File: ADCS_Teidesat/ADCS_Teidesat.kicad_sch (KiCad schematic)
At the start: 27 parts, among them IC2 L86-M33, IC3 MAX2659ELT+T, IC4 THVD1400DR, IC5 TMS5703137DPGEQQ1, IC7 LSM6DSV16XTR, IC8 LIS2MDLTR, Y1 ATX-H13-F-16.000MHz-G100-T

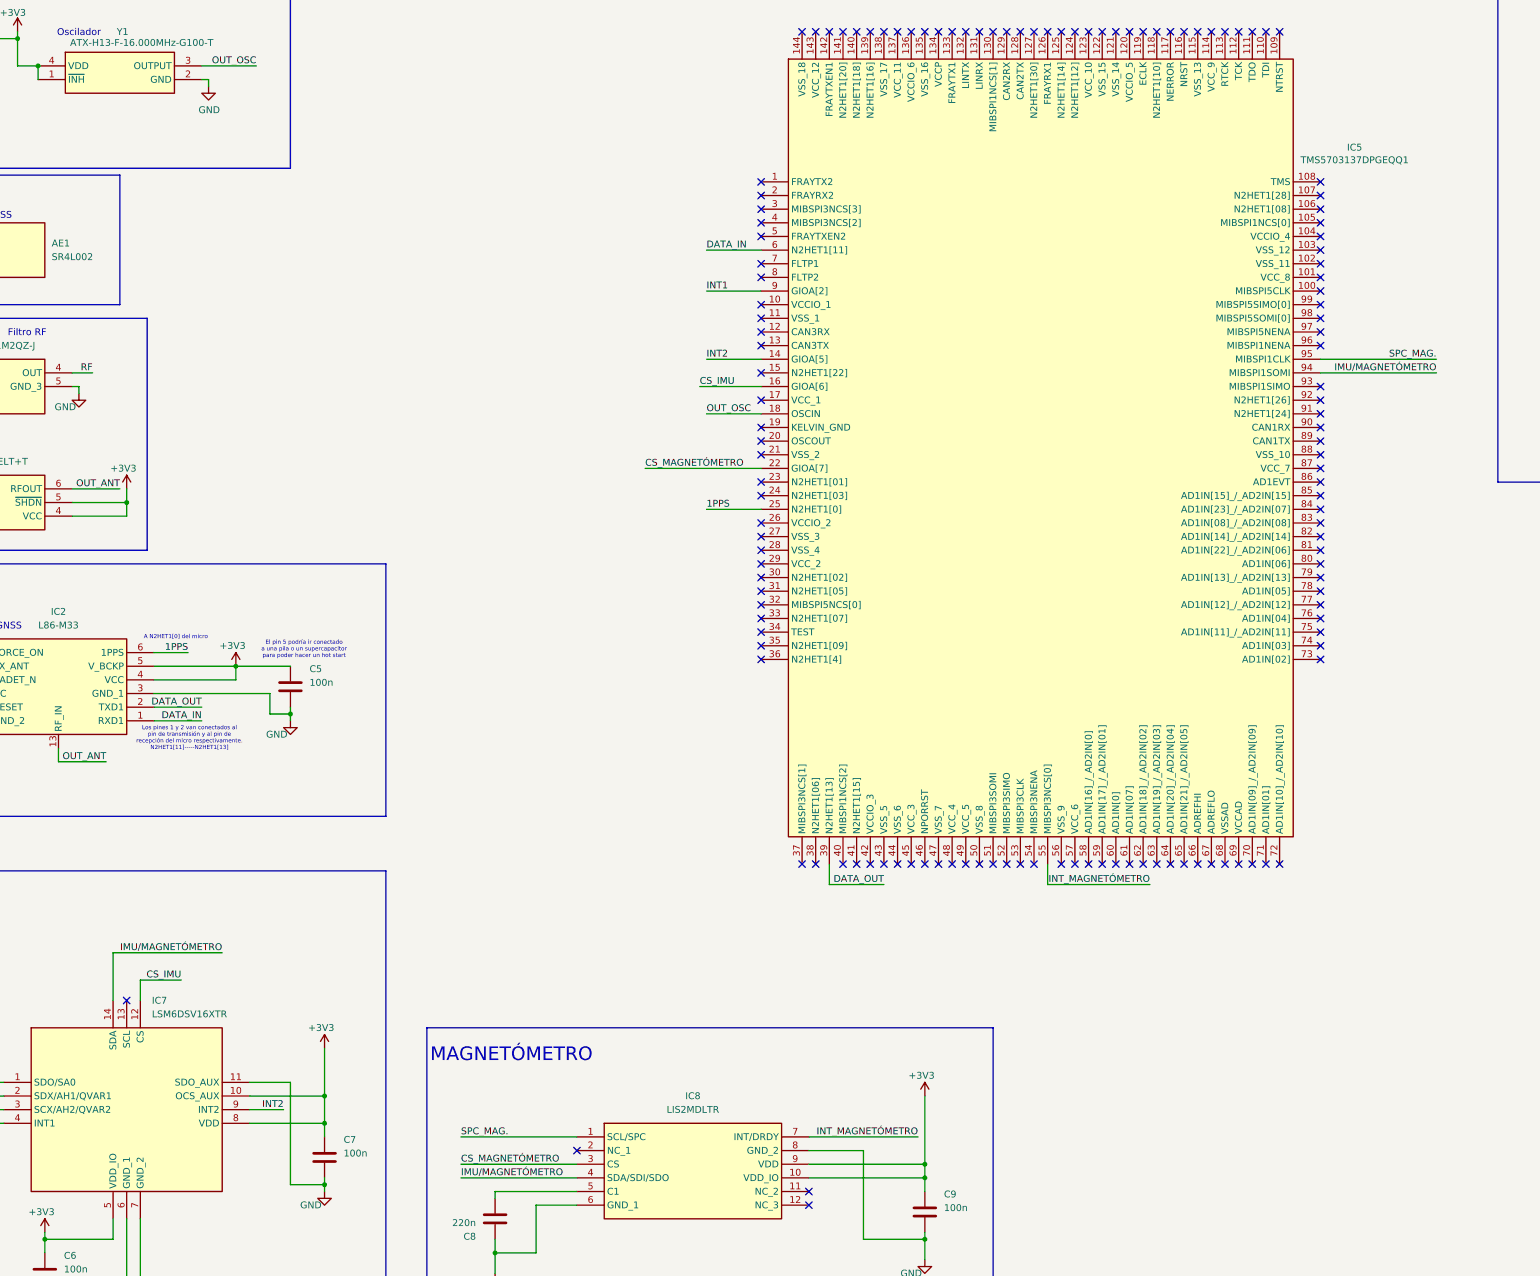
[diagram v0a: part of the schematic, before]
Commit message: Corrección en de los Pines 13 y 14 de la IMU
He corregido el Pin 13 (SCL) y el Pin 14 (SDA) de la IMU según su datasheet. Además, he pasado la línea compartida entre la IMU y el magnetómetro a una única línea para este último
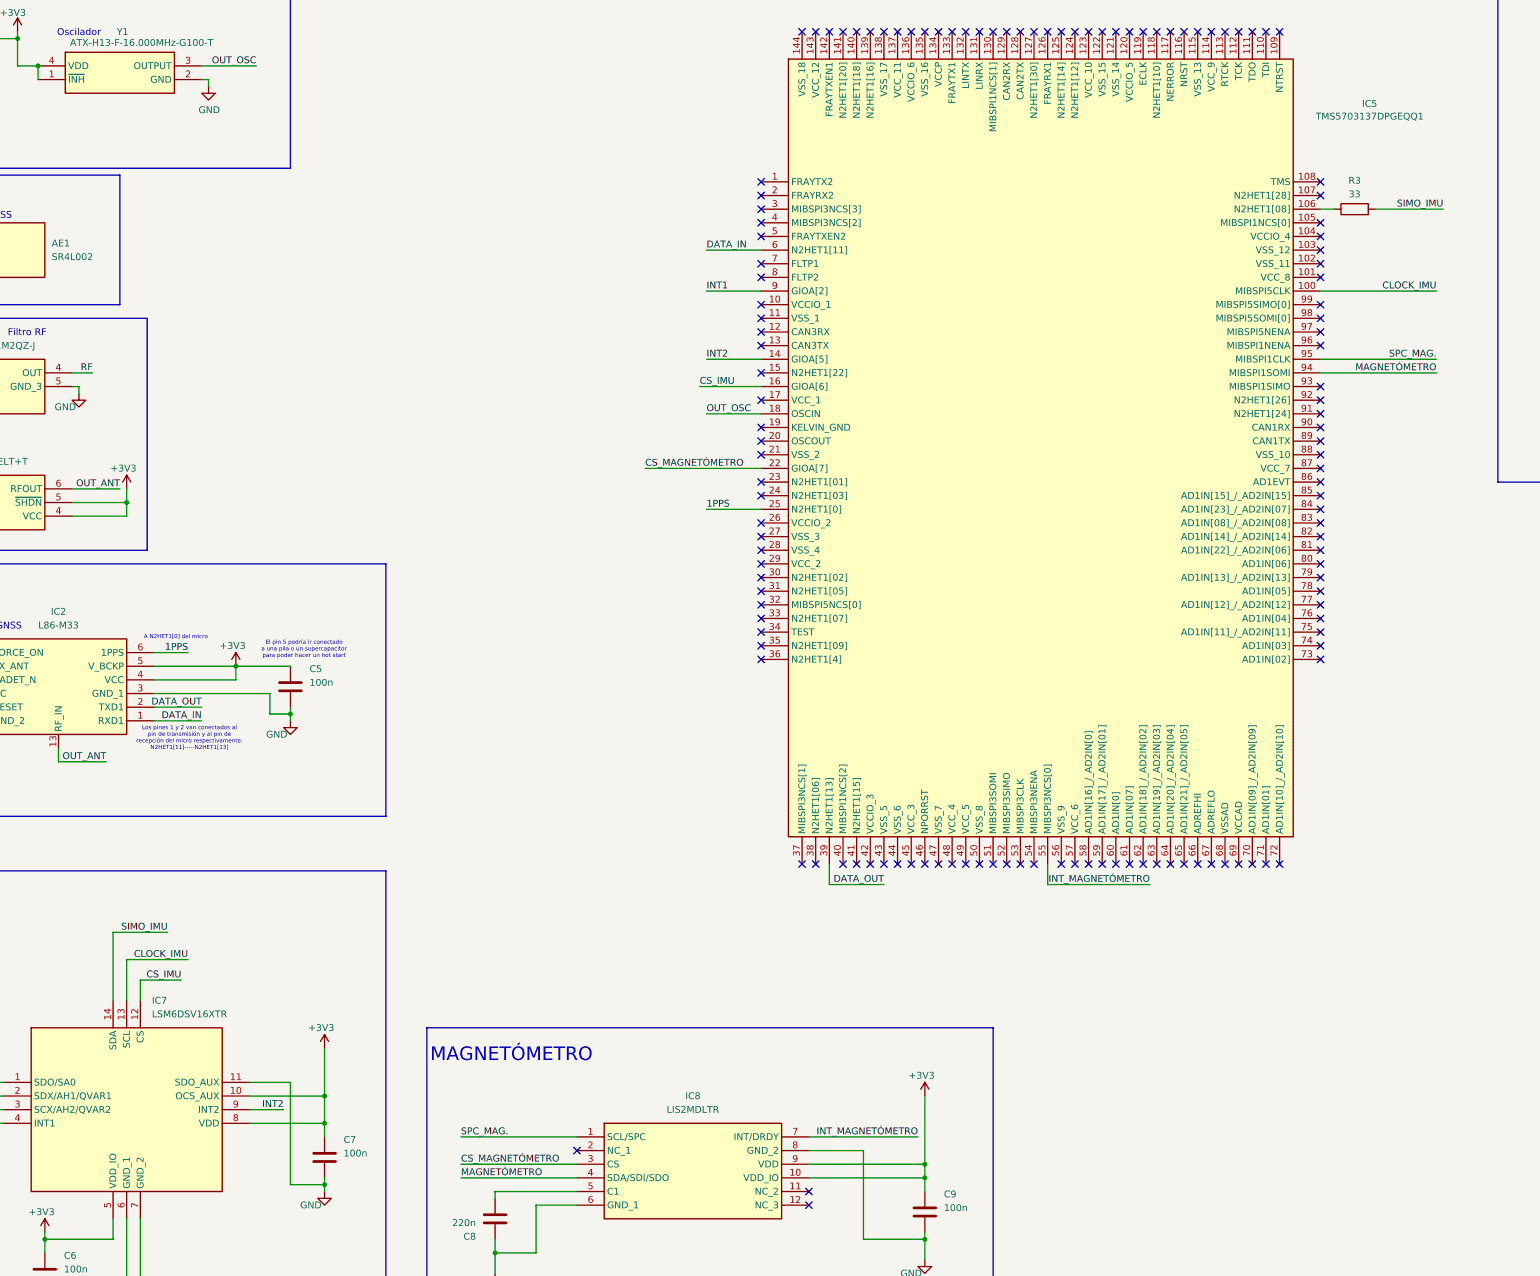
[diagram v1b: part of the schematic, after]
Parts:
- added R3: 33, Resistor_SMD:R_0201_0603Metric, symbol Device:R
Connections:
- net CLOCK_IMU: now reaches IC7.13 (SCL)
- net CLOCK_IMU: now also IC5.100 (MIBSPI5CLK)
- net at IC5.106 (N2HET1[08]): now also R3.1
- net IMU/MAGNETÓMETRO renamed MAGNETÓMETRO
- net MAGNETÓMETRO: no longer IC7.14 (SDA)
- new net SIMO_IMU: IC7.14 (SDA), R3.2
- no-connect marks 242 -> 239
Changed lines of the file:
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@@
 	)
 	(no_connect
-		(at 288.29 60.96)
-	)
-	(no_connect
 		(at 356.87 101.6)
 	)
@@
 	)
 	(no_connect
-		(at 66.04 208.28)
-	)
-	(no_connect
 		(at 356.87 43.18)
 	)
@@
 	)
 	(no_connect
-		(at 288.29 93.98)
-	)
-	(no_connect
 		(at 356.87 93.98)
 	)
@@
 	)
 	(no_connect
-		(at 288.29 76.2)
-	)
-	(no_connect
 		(at 184.15 132.08)
 	)
@@
 	)
 	(no_connect
+		(at 288.29 93.98)
+	)
+	(no_connect
 		(at 356.87 88.9)
 	)
@@
 	(wire
 		(pts
-			(xy 63.5 199.39) (xy 63.5 208.28)
+			(xy 298.45 60.96) (xy 311.15 60.96)
+		)
+		(stroke
+			(width 0)
+			(type default)
+		)
+	)
+	(wire
+		(pts
+			(xy 63.5 195.58) (xy 63.5 208.28)
 		)
 		(stroke
@@
 	(wire
 		(pts
-			(xy 83.82 199.39) (xy 63.5 199.39)
+			(xy 73.66 195.58) (xy 63.5 195.58)
 		)
 		(stroke
@@
 	(wire
 		(pts
+			(xy 288.29 76.2) (xy 309.88 76.2)
+		)
+		(stroke
+			(width 0)
+			(type default)
+		)
+	)
+	(wire
+		(pts
 			(xy 196.85 186.69) (xy 196.85 182.88)
 		)
@@
 	(wire
 		(pts
+			(xy 66.04 200.66) (xy 77.47 200.66)
+		)
+		(stroke
+			(width 0)
+			(type default)
+		)
+	)
+	(wire
+		(pts
 			(xy 25.4 115.57) (xy 20.32 115.57)
 		)
@@
 	(wire
 		(pts
-			(xy 288.29 91.44) (xy 309.88 91.44)
+			(xy 66.04 208.28) (xy 66.04 200.66)
 		)
 		(stroke
@@
 	(wire
 		(pts
+			(xy 309.88 91.44) (xy 288.29 91.44)
+		)
+		(stroke
+			(width 0)
+			(type default)
+		)
+	)
+	(wire
+		(pts
 			(xy 49.53 34.29) (xy 49.53 36.83)
 		)
@@
 	(wire
 		(pts
+			(xy 288.29 60.96) (xy 290.83 60.96)
+		)
+		(stroke
+			(width 0)
+			(type default)
+		)
+	)
+	(wire
+		(pts
 			(xy 81.28 36.83) (xy 81.28 38.1)
 		)
@@
 		)
 	)
+	(label "MAGNETÓMETRO"
+		(at 309.88 91.44 180)
+		(effects
+			(font
+				(size 1.27 1.27)
+			)
+			(justify right bottom)
+		)
+	)
 	(label "OUT_OSC"
 		(at 173.99 99.06 0)
@@
 		)
 	)
+	(label "CLOCK_IMU"
+		(at 309.88 76.2 180)
+		(effects
+			(font
+				(size 1.27 1.27)
+			)
+			(justify right bottom)
+		)
+	)
+	(label "SIMO_IMU"
+		(at 311.15 60.96 180)
+		(effects
+			(font
+				(size 1.27 1.27)
+			)
+			(justify right bottom)
+		)
+	)
 	(label "ANTENNA"
 		(at 16.51 66.04 0)
@@
 		)
 	)
+	(label "CLOCK_IMU"
+		(at 77.47 200.66 180)
+		(effects
+			(font
+				(size 1.27 1.27)
+			)
+			(justify right bottom)
+		)
+	)
 	(label "OUT_OSC"
 		(at 90.17 34.29 180)
@@
 		)
 	)
-	(label "IMU{slash}MAGNETÓMETRO"
+	(label "MAGNETÓMETRO"
 		(at 128.27 241.3 0)
 		(effects
@@
 		)
 	)
-	(label "IMU{slash}MAGNETÓMETRO"
-		(at 309.88 91.44 180)
-		(effects
-			(font
-				(size 1.27 1.27)
-			)
-			(justify right bottom)
-		)
-	)
 	(label "INT1"
 		(at 34.29 231.14 0)
@@
 		)
 	)
-	(label "IMU{slash}MAGNETÓMETRO"
-		(at 83.82 199.39 180)
+	(label "SIMO_IMU"
+		(at 73.66 195.58 180)
 		(effects
 			(font
@@
 		(dnp no)
 		(property "Reference" "IC5"
-			(at 294.64 49.4598 0)
+			(at 297.434 41.3318 0)
 			(effects
 				(font
@@
 		)
 		(property "Value" "TMS5703137DPGEQQ1"
-			(at 294.64 51.816 0)
+			(at 297.434 43.688 0)
 			(effects
 				(font
@@
 					(unit 1)
 				)
+			)
+		)
+	)
+	(symbol
+		(lib_id "Device:R")
+		(at 294.64 60.96 90)
+		(unit 1)
+		(exclude_from_sim no)
+		(in_bom yes)
+		(on_board yes)
+		(dnp no)
+		(property "Reference" "R3"
+			(at 294.64 55.626 90)
+			(effects
+				(font
+					(size 1.27 1.27)
+				)
+			)
+		)
+		(property "Value" "33"
+			(at 294.64 58.166 90)
+			(effects
+				(font
+					(size 1.27 1.27)
+				)
+			)
+		)
+		(property "Footprint" "Resistor_SMD:R_0201_0603Metric"
+			(at 294.64 62.738 90)
+			(effects
+				(font
+					(size 1.27 1.27)
+				)
+				(hide yes)
+			)
+		)
+		(property "Datasheet" "~"
+			(at 294.64 60.96 0)
+			(effects
+				(font
+					(size 1.27 1.27)
+				)
+				(hide yes)
+			)
+		)
+		(property "Description" "Resistor"
+			(at 294.64 60.96 0)
+			(effects
+				(font
+					(size 1.27 1.27)
+				)
+				(hide yes)
+			)
+		)
+		(pin "1"
+		)
+		(pin "2"
+		)
+		(instances
+			(project "ADCS_Teidesat"
+				(path "/983c426c-24e0-4c65-ab69-1f1824adc5c6"
+					(reference "R3")
+					(unit 1)
+				)

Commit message: Arreglo problemas de plantilla
Arreglamos problemas en la plantilla y realizamos ciertas correcciones de Salvador

Co-Authored-By: hugohdezmo <238262256+hugohdezmo@users.noreply.github.com>
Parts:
- removed C8: 220n, Capacitor_SMD:C_0805_2012Metric, symbol Device:C
- removed C9: 100n, Capacitor_SMD:C_0805_2012Metric, symbol Device:C
- removed IC4: THVD1400DR, Huellas ADCS:SOIC127P600X175-8N, symbol THVD1400DR:THVD1400DR
- removed R2: 10k, Resistor_SMD:R_0201_0603Metric, symbol Device:R
- added C3, C5: 100n, Capacitor_SMD:C_0805_2012Metric, symbol Device:C
- added R1: 10k, Resistor_SMD:R_0201_0603Metric, symbol Device:R
- C6: value 100n -> 220n
- renumbered C11 to C1, C3 to C10, C4 to C11, C10 to C2, C5 to C4, C1 to C8, C2 to C9, R1 to R2, IC3 to U1, IC2 to U2, IC7 to U3, IC8 to U4, IC5 to U5
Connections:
- net +3V3: now also C3.1, C5.1, R1.1; no longer C6.1
- net GND: now also C6.1, C3.2, C5.2, R1.2; no longer C6.2
- net at U4.5 (C1): now also C6.2
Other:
- note removed: "Interfaz digital hacia OBC"
- moved on the sheet: AE1, C1, C10, C11, C2, C4, C8, C9, H1, H2, MH1, MH2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
